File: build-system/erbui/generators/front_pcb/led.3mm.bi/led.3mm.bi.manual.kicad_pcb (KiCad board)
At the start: 2 copper layers, 2 parts

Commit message: Update pcbs
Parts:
- removed Pin0: TestPoint, TestPoint:TestPoint_Pad_D1.5mm
- ZZ1: value IN -> LED_Dual_ACA; footprint Connector_Thonk:ThonkiconnJack -> LED_THT:LED_D3.0mm-3
- moved ZZ1 2.54 mm to (-2.54, 0.00)
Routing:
- net Net-(Pin0-Pad1): track 1.92 -> 0.00 mm
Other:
- board text removed: "pin"
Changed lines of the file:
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@@
   (general
     (thickness 1.6)
-    (drawings 1)
-    (tracks 1)
+    (drawings 0)
+    (tracks 0)
     (zones 0)
-    (modules 2)
-    (nets 3)
+    (modules 1)
+    (nets 4)
   )
   (page A4)
@@
     (uvia_min_drill 0.1)
     (edge_width 0.15)
-    (segment_width 0.2)
+    (segment_width 0.15)
     (pcb_text_width 0.3)
     (pcb_text_size 1.5 1.5)
@@
     (mod_text_size 1 1)
     (mod_text_width 0.15)
-    (pad_size 2.2 1.3)
-    (pad_drill 1.5)
+    (pad_size 1.8 1.8)
+    (pad_drill 0.9)
     (pad_to_mask_clearance 0.2)
     (aux_axis_origin 0 0)
@@
   (net 1 GND)
   (net 2 "Net-(Pin0-Pad1)")
+  (net 3 "Net-(Pin1-Pad1)")
   (net_class Default "This is the default net class."
     (clearance 0.1524)
@@
     (add_net GND)
     (add_net "Net-(Pin0-Pad1)")
+    (add_net "Net-(Pin1-Pad1)")
   )
-  (module Connector_Thonk:ThonkiconnJack locked (layer F.Cu)
-    (at 0 0)
-    (fp_text reference ZZ1 (at 0 -7.5) (layer F.SilkS) hide
+  (module LED_THT:LED_D3.0mm-3 locked (layer F.Cu)
+    (at -2.54 0)
+    (descr "LED, diameter 3.0mm, 2 pins, diameter 3.0mm, 3 pins, http://www.kingbright.com/attachments/file/psearch/000/00/00/L-3VSURKCGKC(Ver.8A).pdf")
+    (tags "LED diameter 3.0mm 2 pins diameter 3.0mm 3 pins")
+    (fp_text reference ZZ1 (at 2.54 -2.96) (layer F.SilkS) hide
       (effects (font (size 1 1) (thickness 0.15)))
     )
-    (fp_text value IN (at 0 9.3) (layer F.Fab)
+    (fp_text value LED_Dual_ACA (at 2.54 2.96) (layer F.Fab)
       (effects (font (size 1 1) (thickness 0.15)))
     )
-    (fp_circle (center 0 0) (end 1.8 0) (layer F.SilkS) (width 0.15))
-    (fp_line (start -4.5 -6) (end 4.5 -6) (layer F.SilkS) (width 0.15))
-    (fp_line (start -4.5 -6) (end -4.5 4.5) (layer F.SilkS) (width 0.15))
-    (fp_line (start 4.5 -6) (end 4.5 4.5) (layer F.SilkS) (width 0.15))
-    (fp_line (start -4.5 4.5) (end 4.5 4.5) (layer F.SilkS) (width 0.15))
-    (pad "" np_thru_hole circle (at 0 0) (size 2.5 2.5) (drill 2.5) (layers *.Cu *.Mask))
-    (pad T thru_hole oval (at 0 -4.92) (size 2.2 1.2) (drill oval 1.5 0.5) (layers *.Cu *.Mask)
+    (fp_line (start 6.25 -2.25) (end -1.15 -2.25) (layer F.CrtYd) (width 0.05))
+    (fp_line (start 6.25 2.25) (end 6.25 -2.25) (layer F.CrtYd) (width 0.05))
+    (fp_line (start -1.15 2.25) (end 6.25 2.25) (layer F.CrtYd) (width 0.05))
+    (fp_line (start -1.15 -2.25) (end -1.15 2.25) (layer F.CrtYd) (width 0.05))
+    (fp_line (start 0.98 1.08) (end 0.98 1.236) (layer F.SilkS) (width 0.12))
+    (fp_line (start 0.98 -1.236) (end 0.98 -1.08) (layer F.SilkS) (width 0.12))
+    (fp_line (start 1.04 -1.16619) (end 1.04 1.16619) (layer F.Fab) (width 0.1))
+    (fp_circle (center 2.54 0) (end 4.04 0) (layer F.Fab) (width 0.1))
+    (fp_arc (start 2.54 0) (end 1.04 -1.16619) (angle 284.3) (layer F.Fab) (width 0.1))
+    (fp_arc (start 2.54 0) (end 0.98 -1.235516) (angle 108.8) (layer F.SilkS) (width 0.12))
+    (fp_arc (start 2.54 0) (end 0.98 1.235516) (angle -108.8) (layer F.SilkS) (width 0.12))
+    (fp_arc (start 2.54 0) (end 1.499039 -1.08) (angle 87.9) (layer F.SilkS) (width 0.12))
+    (fp_arc (start 2.54 0) (end 1.499039 1.08) (angle -87.9) (layer F.SilkS) (width 0.12))
+    (pad 1 thru_hole circle (at 0 0) (size 1.8 1.8) (drill 0.9) (layers *.Cu *.Mask)
       (net 2 "Net-(Pin0-Pad1)"))
-    (pad TN thru_hole oval (at 0 3.38) (size 2.2 1.3) (drill oval 1.5 0.6) (layers *.Cu *.Mask)
+    (pad 2 thru_hole rect (at 2.54 0) (size 1.8 1.8) (drill 0.9) (layers *.Cu *.Mask)
       (net 1 GND))
-    (pad S thru_hole oval (at 0 6.48) (size 2 1.3) (drill oval 1.3 0.6) (layers *.Cu *.Mask)
-      (net 1 GND))
+    (pad 3 thru_hole circle (at 5.08 0) (size 1.8 1.8) (drill 0.9) (layers *.Cu *.Mask)
+      (net 3 "Net-(Pin1-Pad1)"))
+    (model ${KISYS3DMOD}/LED_THT.3dshapes/LED_D3.0mm-3.wrl
+      (at (xyz 0 0 0))
+      (scale (xyz 1 1 1))
+      (rotate (xyz 0 0 0))
+    )
   )
-  (module TestPoint:TestPoint_Pad_D1.5mm (layer B.Cu)
-    (at 0 -3)
-    (descr "SMD pad as test Point, diameter 1.5mm")
-    (tags "test point SMD pad")
-    (attr virtual)
-    (fp_text reference Pin0 (at 0 1.648) (layer F.SilkS) hide
-      (effects (font (size 1 1) (thickness 0.15)))
-    )
-    (fp_text value TestPoint (at 0 -1.75) (layer B.Fab)
-      (effects (font (size 1 1) (thickness 0.15)) (justify mirror))
-    )
-    (fp_circle (center 0 0) (end 0 -0.95) (layer B.SilkS) (width 0.12))
-    (fp_circle (center 0 0) (end 1.25 0) (layer B.CrtYd) (width 0.05))
-    (fp_text user %R (at 0 1.65) (layer B.Fab)
-      (effects (font (size 1 1) (thickness 0.15)) (justify mirror))
-    )
-    (pad 1 smd circle (at 0 0) (size 1.5 1.5) (layers B.Cu B.Mask)
-      (net 2 "Net-(Pin0-Pad1)"))
-  )
-  (gr_text pin (at -0.95 -3) (layer B.SilkS)
-    (effects (font (size 1 1) (thickness 0.15)) (justify left mirror))
-  )
-  (segment (start 0 -4.92) (end 0 -3) (width 0.635) (layer B.Cu) (net 2))
 )

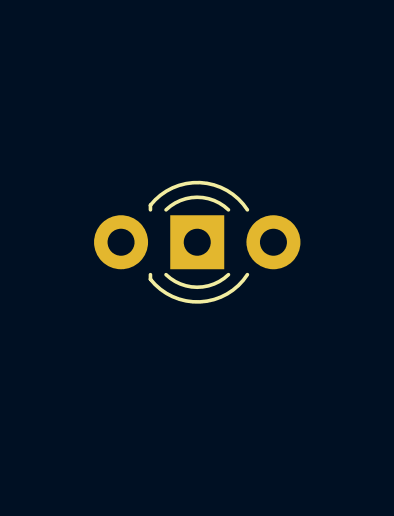
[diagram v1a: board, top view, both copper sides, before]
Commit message: Show reference name on silkscreen for all controls
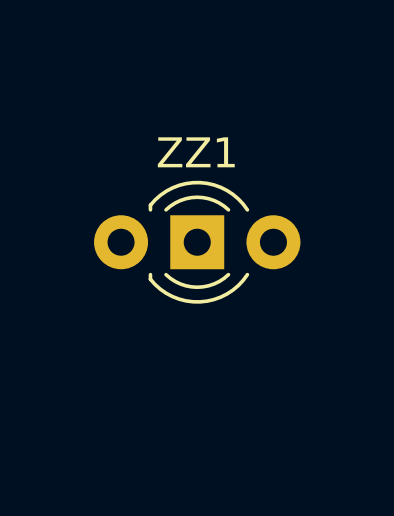
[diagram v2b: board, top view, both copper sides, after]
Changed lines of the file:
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@@
     (descr "LED, diameter 3.0mm, 2 pins, diameter 3.0mm, 3 pins, http://www.kingbright.com/attachments/file/psearch/000/00/00/L-3VSURKCGKC(Ver.8A).pdf")
     (tags "LED diameter 3.0mm 2 pins diameter 3.0mm 3 pins")
-    (fp_text reference ZZ1 (at 2.54 -2.96) (layer F.SilkS) hide
+    (fp_text reference ZZ1 (at 2.54 -2.96) (layer F.SilkS)
       (effects (font (size 1 1) (thickness 0.15)))
     )
